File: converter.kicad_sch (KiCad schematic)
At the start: 10 parts, among them U401 XL4015

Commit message: PCB layout added
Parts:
- C420: footprint (none) -> Capacitor_SMD:CP_Elec_8x10.5
- C421: footprint (none) -> Capacitor_SMD:CP_Elec_10x10.5
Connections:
- net +12V: now reaches C418.1, C419.1, C421.1, U401.5 (VIN)
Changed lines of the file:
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@@
+	)
+	(junction
+		(at 86.36 69.85)
+		(diameter 0)
+		(color 0 0 0 0)
 	)
 	(junction
@@
 	(wire
 		(pts
-			(xy 82.55 69.85) (xy 99.06 69.85)
+			(xy 82.55 69.85) (xy 86.36 69.85)
 		)
 		(stroke
@@
 	(wire
 		(pts
+			(xy 86.36 69.85) (xy 99.06 69.85)
+		)
+		(stroke
+			(width 0)
+			(type default)
+		)
+	)
+	(wire
+		(pts
 			(xy 152.4 69.85) (xy 154.94 69.85)
 		)
@@
 		(pts
 			(xy 190.5 78.74) (xy 194.31 78.74)
+		)
+		(stroke
+			(width 0)
+			(type default)
+		)
+	)
+	(wire
+		(pts
+			(xy 86.36 64.77) (xy 86.36 69.85)
 		)
 		(stroke
@@
 			)
 		)
-		(property "Footprint" ""
+		(property "Footprint" "Capacitor_SMD:CP_Elec_8x10.5"
 			(at 173.0248 77.47 0)
 			(effects
@@
 			)
 		)
-		(property "Footprint" ""
+		(property "Footprint" "Capacitor_SMD:CP_Elec_10x10.5"
 			(at 83.5152 77.47 0)
 			(effects
@@
 					(unit 1)
 				)
+			)
+		)
+	)
+	(symbol
+		(lib_id "power:+12V")
+		(at 86.36 64.77 0)
+		(mirror y)
+		(unit 1)
+		(exclude_from_sim no)
+		(in_bom yes)
+		(on_board yes)
+		(dnp no)
+		(property "Reference" "#PWR0400"
+			(at 86.36 68.58 0)
+			(effects
+				(font
+					(size 1.27 1.27)
+				)
+				(hide yes)
+			)
+		)
+		(property "Value" "+12V"
+			(at 86.36 60.96 0)
+			(effects
+				(font
+					(size 1.27 1.27)
+				)
+			)
+		)
+		(property "Footprint" ""
+			(at 86.36 64.77 0)
+			(effects
+				(font
+					(size 1.27 1.27)
+				)
+				(hide yes)
+			)
+		)
+		(property "Datasheet" ""
+			(at 86.36 64.77 0)
+			(effects
+				(font
+					(size 1.27 1.27)
+				)
+				(hide yes)
+			)
+		)
+		(property "Description" "Power symbol creates a global label with name \"+12V\""
+			(at 86.36 64.77 0)
+			(effects
+				(font
+					(size 1.27 1.27)
+				)
+				(hide yes)
+			)
+		)
+		(pin "1"
+		)
+		(instances
+			(project "TPB"
+				(path "/090a8e41-87a8-4fb1-998b-60a2c0dc4cee/586b059c-8adb-4b5f-91ef-9fff6d0411fe"
+					(reference "#PWR0400")
+					(unit 1)
+				)

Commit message: Improve to traces
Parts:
- added C400: 33nF, PCM_JLCPCB:C_0603, symbol PCM_JLCPCB-Capacitors:0603,33nF
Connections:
- net +5V_STDBY: now also C400.1
- net Feedback renamed FB
- net FB: now also C400.2

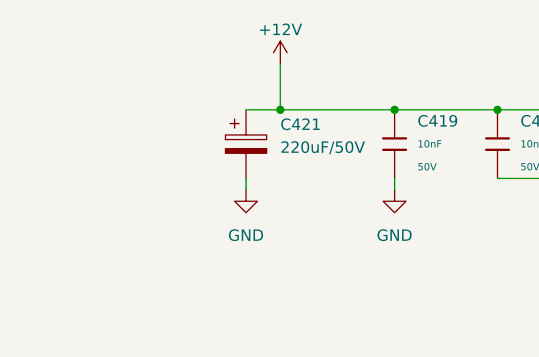
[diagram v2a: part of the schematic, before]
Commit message: Add XT60PW-F and Implement
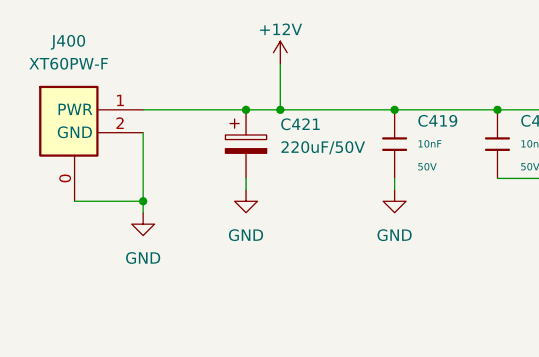
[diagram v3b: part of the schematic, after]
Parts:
- added J400: XT60PW-F, XT60PWF, symbol XT60PW-F:XT60PW-F
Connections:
- net +12V: now also J400.1 (PWR)
- net GND: now also J400.0, J400.2 (GND)
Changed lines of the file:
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@@
+	)
+	(junction
+		(at 82.55 69.85)
+		(diameter 0)
+		(color 0 0 0 0)
 	)
 	(junction
@@
 	)
 	(junction
+		(at 71.12 80.01)
+		(diameter 0)
+		(color 0 0 0 0)
+	)
+	(junction
 		(at 163.83 69.85)
 		(diameter 0)
@@
 	(wire
 		(pts
+			(xy 71.12 81.28) (xy 71.12 80.01)
+		)
+		(stroke
+			(width 0)
+			(type default)
+		)
+	)
+	(wire
+		(pts
 			(xy 110.49 77.47) (xy 118.11 77.47)
 		)
@@
 	(wire
 		(pts
+			(xy 71.12 72.39) (xy 71.12 80.01)
+		)
+		(stroke
+			(width 0)
+			(type default)
+		)
+	)
+	(wire
+		(pts
 			(xy 152.4 69.85) (xy 152.4 72.39)
 		)
@@
 	(wire
 		(pts
+			(xy 71.12 69.85) (xy 82.55 69.85)
+		)
+		(stroke
+			(width 0)
+			(type default)
+		)
+	)
+	(wire
+		(pts
 			(xy 118.11 77.47) (xy 118.11 74.93)
 		)
@@
 		(pts
 			(xy 190.5 87.63) (xy 190.5 88.9)
+		)
+		(stroke
+			(width 0)
+			(type default)
+		)
+	)
+	(wire
+		(pts
+			(xy 71.12 80.01) (xy 63.5 80.01)
 		)
 		(stroke
@@
 	)
 	(symbol
+		(lib_id "XT60PW-F:XT60PW-F")
+		(at 48.26 69.85 0)
+		(unit 1)
+		(exclude_from_sim no)
+		(in_bom yes)
+		(on_board yes)
+		(dnp no)
+		(fields_autoplaced yes)
+		(property "Reference" "J400"
+			(at 62.865 62.23 0)
+			(effects
+				(font
+					(size 1.27 1.27)
+				)
+			)
+		)
+		(property "Value" "XT60PW-F"
+			(at 62.865 64.77 0)
+			(effects
+				(font
+					(size 1.27 1.27)
+				)
+			)
+		)
+		(property "Footprint" "XT60PWF"
+			(at 67.31 164.77 0)
+			(effects
+				(font
+					(size 1.27 1.27)
+				)
+				(justify left top)
+				(hide yes)
+			)
+		)
+		(property "Datasheet" "https://www.tme.eu/Document/1191bc2fa3aee3c446e5a895fd8f7983/XT60PW-F.pdf"
+			(at 67.31 264.77 0)
+			(effects
+				(font
+					(size 1.27 1.27)
+				)
+				(justify left top)
+				(hide yes)
+			)
+		)
+		(property "Description" "Socket; DC supply; XT60; female; PIN: 2; on PCBs; THT; Colour: yellow"
+			(at 54.61 61.468 0)
+			(effects
+				(font
+					(size 1.27 1.27)
+				)
+				(hide yes)
+			)
+		)
+		(property "Height" "8.4"
+			(at 67.31 464.77 0)
+			(effects
+				(font
+					(size 1.27 1.27)
+				)
+				(justify left top)
+				(hide yes)
+			)
+		)
+		(property "TME Electronic Components Part Number" ""
+			(at 67.31 564.77 0)
+			(effects
+				(font
+					(size 1.27 1.27)
+				)
+				(justify left top)
+				(hide yes)
+			)
+		)
+		(property "TME Electronic Components Price/Stock" ""
+			(at 67.31 664.77 0)
+			(effects
+				(font
+					(size 1.27 1.27)
+				)
+				(justify left top)
+				(hide yes)
+			)
+		)
+		(property "Manufacturer_Name" "Amass"
+			(at 67.31 764.77 0)
+			(effects
+				(font
+					(size 1.27 1.27)
+				)
+				(justify left top)
+				(hide yes)
+			)
+		)
+		(property "Manufacturer_Part_Number" "XT60PW-F"
+			(at 67.31 864.77 0)
+			(effects
+				(font
+					(size 1.27 1.27)
+				)
+				(justify left top)
+				(hide yes)
+			)
+		)
+		(pin "1"
+		)
+		(pin "2"
+		)
+		(pin "0"
+		)
+		(instances
+			(project ""
+				(path "/090a8e41-87a8-4fb1-998b-60a2c0dc4cee/586b059c-8adb-4b5f-91ef-9fff6d0411fe"
+					(reference "J400")
+					(unit 1)
+				)
+			)
+		)
+	)
+	(symbol
 		(lib_id "power:+5V")
 		(at 196.85 68.58 0)
@@
 					(unit 1)
 				)
+			)
+		)
+	)
+	(symbol
+		(lib_id "power:GND")
+		(at 71.12 81.28 0)
+		(unit 1)
+		(exclude_from_sim no)
+		(in_bom yes)
+		(on_board yes)
+		(dnp no)
+		(fields_autoplaced yes)
+		(property "Reference" "#PWR0401"
+			(at 71.12 87.63 0)
+			(effects
+				(font
+					(size 1.27 1.27)
+				)
+				(hide yes)
+			)
+		)
+		(property "Value" "GND"
+			(at 71.12 86.36 0)
+			(effects
+				(font
+					(size 1.27 1.27)
+				)
+			)
+		)
+		(property "Footprint" ""
+			(at 71.12 81.28 0)
+			(effects
+				(font
+					(size 1.27 1.27)
+				)
+				(hide yes)
+			)
+		)
+		(property "Datasheet" ""
+			(at 71.12 81.28 0)
+			(effects
+				(font
+					(size 1.27 1.27)
+				)
+				(hide yes)
+			)
+		)
+		(property "Description" "Power symbol creates a global label with name \"GND\" , ground"
+			(at 71.12 81.28 0)
+			(effects
+				(font
+					(size 1.27 1.27)
+				)
+				(hide yes)
+			)
+		)
+		(pin "1"
+		)
+		(instances
+			(project "TPB"
+				(path "/090a8e41-87a8-4fb1-998b-60a2c0dc4cee/586b059c-8adb-4b5f-91ef-9fff6d0411fe"
+					(reference "#PWR0401")
+					(unit 1)
+				)

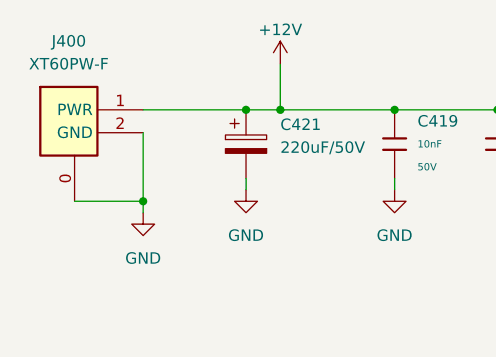
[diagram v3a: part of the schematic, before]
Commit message: change LED Indicator
also most wide tracks changed to polygons
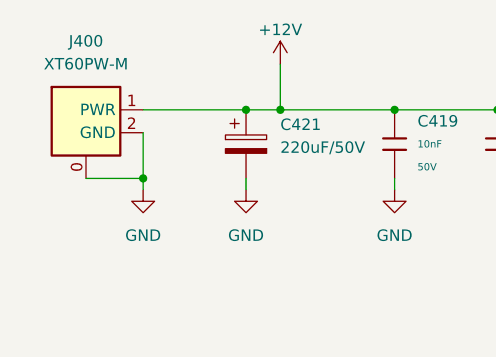
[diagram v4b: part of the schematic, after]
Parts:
- removed J400: XT60PW-F, XT60PWF, symbol XT60PW-F:XT60PW-F
- added J400: XT60PW-M, XT60PW-M:XT60PWM, symbol XT60PW-M:XT60PW-M
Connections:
- net +12V: now also J400.1 (PWR)
- net GND: now also J400.0, J400.2 (GND)
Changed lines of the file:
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@@
-	)
-	(junction
-		(at 71.12 80.01)
-		(diameter 0)
-		(color 0 0 0 0)
 	)
 	(junction
@@
 		(color 0 0 0 0)
 	)
+	(junction
+		(at 71.12 77.47)
+		(diameter 0)
+		(color 0 0 0 0)
+	)
 	(wire
 		(pts
@@
 	(wire
 		(pts
+			(xy 64.77 77.47) (xy 71.12 77.47)
+		)
+		(stroke
+			(width 0)
+			(type default)
+		)
+	)
+	(wire
+		(pts
 			(xy 82.55 69.85) (xy 86.36 69.85)
 		)
@@
 	(wire
 		(pts
-			(xy 71.12 81.28) (xy 71.12 80.01)
+			(xy 71.12 72.39) (xy 71.12 77.47)
 		)
 		(stroke
@@
 	(wire
 		(pts
-			(xy 71.12 72.39) (xy 71.12 80.01)
-		)
-		(stroke
-			(width 0)
-			(type default)
-		)
-	)
-	(wire
-		(pts
 			(xy 152.4 69.85) (xy 152.4 72.39)
 		)
@@
 	(wire
 		(pts
-			(xy 71.12 80.01) (xy 63.5 80.01)
-		)
-		(stroke
-			(width 0)
-			(type default)
-		)
-	)
-	(wire
-		(pts
 			(xy 190.5 78.74) (xy 190.5 80.01)
 		)
@@
 		(pts
 			(xy 196.85 68.58) (xy 196.85 69.85)
+		)
+		(stroke
+			(width 0)
+			(type default)
+		)
+	)
+	(wire
+		(pts
+			(xy 71.12 77.47) (xy 71.12 78.74)
 		)
 		(stroke
@@
 	)
 	(symbol
-		(lib_id "XT60PW-F:XT60PW-F")
-		(at 48.26 69.85 0)
-		(unit 1)
-		(exclude_from_sim no)
-		(in_bom yes)
-		(on_board yes)
-		(dnp no)
-		(fields_autoplaced yes)
-		(property "Reference" "J400"
-			(at 62.865 62.23 0)
-			(effects
-				(font
-					(size 1.27 1.27)
-				)
-			)
-		)
-		(property "Value" "XT60PW-F"
-			(at 62.865 64.77 0)
-			(effects
-				(font
-					(size 1.27 1.27)
-				)
-			)
-		)
-		(property "Footprint" "XT60PWF"
-			(at 67.31 164.77 0)
-			(effects
-				(font
-					(size 1.27 1.27)
-				)
-				(justify left top)
-				(hide yes)
-			)
-		)
-		(property "Datasheet" "https://www.tme.eu/Document/1191bc2fa3aee3c446e5a895fd8f7983/XT60PW-F.pdf"
-			(at 67.31 264.77 0)
-			(effects
-				(font
-					(size 1.27 1.27)
-				)
-				(justify left top)
-				(hide yes)
-			)
-		)
-		(property "Description" "Socket; DC supply; XT60; female; PIN: 2; on PCBs; THT; Colour: yellow"
-			(at 54.61 61.468 0)
-			(effects
-				(font
-					(size 1.27 1.27)
-				)
-				(hide yes)
-			)
-		)
-		(property "Height" "8.4"
-			(at 67.31 464.77 0)
-			(effects
-				(font
-					(size 1.27 1.27)
-				)
-				(justify left top)
-				(hide yes)
-			)
-		)
-		(property "TME Electronic Components Part Number" ""
-			(at 67.31 564.77 0)
-			(effects
-				(font
-					(size 1.27 1.27)
-				)
-				(justify left top)
-				(hide yes)
-			)
-		)
-		(property "TME Electronic Components Price/Stock" ""
-			(at 67.31 664.77 0)
-			(effects
-				(font
-					(size 1.27 1.27)
-				)
-				(justify left top)
-				(hide yes)
-			)
-		)
-		(property "Manufacturer_Name" "Amass"
-			(at 67.31 764.77 0)
-			(effects
-				(font
-					(size 1.27 1.27)
-				)
-				(justify left top)
-				(hide yes)
-			)
-		)
-		(property "Manufacturer_Part_Number" "XT60PW-F"
-			(at 67.31 864.77 0)
-			(effects
-				(font
-					(size 1.27 1.27)
-				)
-				(justify left top)
-				(hide yes)
-			)
-		)
-		(pin "1"
-		)
-		(pin "2"
-		)
-		(pin "0"
-		)
-		(instances
-			(project ""
-				(path "/090a8e41-87a8-4fb1-998b-60a2c0dc4cee/586b059c-8adb-4b5f-91ef-9fff6d0411fe"
-					(reference "J400")
-					(unit 1)
-				)
-			)
-		)
-	)
-	(symbol
 		(lib_id "power:+5V")
 		(at 196.85 68.58 0)
@@
 				(path "/090a8e41-87a8-4fb1-998b-60a2c0dc4cee/586b059c-8adb-4b5f-91ef-9fff6d0411fe"
 					(reference "C421")
+					(unit 1)
+				)
+			)
+		)
+	)
+	(symbol
+		(lib_id "XT60PW-M:XT60PW-M")
+		(at 60.96 71.12 0)
+		(unit 1)
+		(exclude_from_sim no)
+		(in_bom yes)
+		(on_board yes)
+		(dnp no)
+		(fields_autoplaced yes)
+		(property "Reference" "J400"
+			(at 64.77 62.23 0)
+			(effects
+				(font
+					(size 1.27 1.27)
+				)
+			)
+		)
+		(property "Value" "XT60PW-M"
+			(at 64.77 64.77 0)
+			(effects
+				(font
+					(size 1.27 1.27)
+				)
+			)
+		)
+		(property "Footprint" "XT60PW-M:XT60PWM"
+			(at 77.47 166.04 0)
+			(effects
+				(font
+					(size 1.27 1.27)
+				)
+				(justify left top)
+				(hide yes)
+			)
+		)
+		(property "Datasheet" "https://www.tme.eu/Document/9b8d0c5eb7094295f3d3112c214d3ade/XT60PW%20SPEC.pdf"
+			(at 77.47 266.04 0)
+			(effects
+				(font
+					(size 1.27 1.27)
+				)
+				(justify left top)
+				(hide yes)
+			)
+		)
+		(property "Description" "Socket; DC supply; XT60; male; PIN: 2; on PCBs; THT; Colour: yellow"
+			(at 64.262 80.518 0)
+			(effects
+				(font
+					(size 1.27 1.27)
+				)
+				(hide yes)
+			)
+		)
+		(property "Height" "8.4"
+			(at 77.47 466.04 0)
+			(effects
+				(font
+					(size 1.27 1.27)
+				)
+				(justify left top)
+				(hide yes)
+			)
+		)
+		(property "TME Electronic Components Part Number" ""
+			(at 77.47 566.04 0)
+			(effects
+				(font
+					(size 1.27 1.27)
+				)
+				(justify left top)
+				(hide yes)
+			)
+		)
+		(property "TME Electronic Components Price/Stock" ""
+			(at 77.47 666.04 0)
+			(effects
+				(font
+					(size 1.27 1.27)
+				)
+				(justify left top)
+				(hide yes)
+			)
+		)
+		(property "Manufacturer_Name" "Changzou Amass Elec"
+			(at 77.47 766.04 0)
+			(effects
+				(font
+					(size 1.27 1.27)
+				)
+				(justify left top)
+				(hide yes)
+			)
+		)
+		(property "Manufacturer_Part_Number" "XT60PW-M"
+			(at 77.47 866.04 0)
+			(effects
+				(font
+					(size 1.27 1.27)
+				)
+				(justify left top)
+				(hide yes)
+			)
+		)
+		(pin "0"
+		)
+		(pin "1"
+		)
+		(pin "2"
+		)
+		(instances
+			(project ""
+				(path "/090a8e41-87a8-4fb1-998b-60a2c0dc4cee/586b059c-8adb-4b5f-91ef-9fff6d0411fe"
+					(reference "J400")
 					(unit 1)
 				)
@@
 	(symbol
 		(lib_id "power:GND")
-		(at 71.12 81.28 0)
+		(at 71.12 78.74 0)
 		(unit 1)
 		(exclude_from_sim no)
@@
 		(fields_autoplaced yes)
 		(property "Reference" "#PWR0401"
-			(at 71.12 87.63 0)
+			(at 71.12 85.09 0)
 			(effects
 				(font
@@
 		)
 		(property "Value" "GND"
-			(at 71.12 86.36 0)
+			(at 71.12 83.82 0)
 			(effects
 				(font
@@
 		)
 		(property "Footprint" ""
-			(at 71.12 81.28 0)
+			(at 71.12 78.74 0)
 			(effects
 				(font
@@
 		)
 		(property "Datasheet" ""
-			(at 71.12 81.28 0)
+			(at 71.12 78.74 0)
 			(effects
 				(font
@@
 		)
 		(property "Description" "Power symbol creates a global label with name \"GND\" , ground"
-			(at 71.12 81.28 0)
-			(effects
-				(font
+			(at 71.12 78.74 0)
+			(effects
+				(font
